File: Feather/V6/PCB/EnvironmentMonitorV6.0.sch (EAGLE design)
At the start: 64 parts, among them IC1 BME680, IC2 TCS3472, IC3 CCS811, IC5 FEATHERWING_NODIM, Q1 IRFML8244TRPBF, U1 GRIDEYE, U2 LMV358, U3 LIS3DH

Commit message: Modified mounting holes to smaller size to match enclosure.
Modified cutout so it's a larger continious section.

Updated images from DirtyPCBs

Added image exports from Eagle.

Boards updated at DirtyPCBs.
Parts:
- removed H1, H2, H3, H4, H5: MOUNT-HOLE2.8, holes:MOUNT-HOLE2.8
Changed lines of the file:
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@@
 <part name="SUPPLY10" library="SparkFun-Aesthetics" deviceset="3.3V" device=""/>
 <part name="C3" library="SparkFun-Capacitors" deviceset="1.0UF-25V-+80/-20(0805)" device="&quot;" value="1.0uF"/>
-<part name="H1" library="holes" deviceset="MOUNT-HOLE" device="2.8" value="MOUNT-HOLE2.8"/>
-<part name="H2" library="holes" deviceset="MOUNT-HOLE" device="2.8" value="MOUNT-HOLE2.8"/>
 <part name="LOGO1" library="SparkFun-Aesthetics" deviceset="OSHW-LOGO" device="M"/>
 <part name="SUPPLY14" library="SparkFun-Aesthetics" deviceset="3.3V" device=""/>
@@
 <part name="SUPPLY5" library="SparkFun-Aesthetics" deviceset="3.3V" device=""/>
 <part name="IC5" library="ThingySticks" deviceset="FEATHERWING" device="_NODIM" value="FEATHERWING_NODIM"/>
-<part name="H3" library="holes" deviceset="MOUNT-HOLE" device="2.8" value="MOUNT-HOLE2.8"/>
-<part name="H4" library="holes" deviceset="MOUNT-HOLE" device="2.8" value="MOUNT-HOLE2.8"/>
 <part name="JP3" library="SparkFun-Connectors" deviceset="M04" device="JST-PTH-VERT" value="Serial"/>
 <part name="JP4" library="SparkFun-Connectors" deviceset="M04" device="JST-PTH-VERT" value="D7-8"/>
@@
 <part name="BT1" library="ThingySticks" deviceset="BATTERY" device="-16340"/>
 <part name="GND19" library="SparkFun-Aesthetics" deviceset="GND" device=""/>
-<part name="H5" library="holes" deviceset="MOUNT-HOLE" device="2.8" value="MOUNT-HOLE2.8"/>
 <part name="U1" library="SparkFun-Sensors" deviceset="GRIDEYE" device=""/>
 <part name="U2" library="SparkFun-IC-Amplifiers" deviceset="LMV358" device="SOIC" value="LMV358"/>
@@
 <instance part="SUPPLY10" gate="G$1" x="119.38" y="96.52"/>
 <instance part="C3" gate="G$1" x="15.24" y="160.02" rot="R180"/>
-<instance part="H1" gate="G$1" x="198.12" y="180.34"/>
-<instance part="H2" gate="G$1" x="198.12" y="175.26"/>
 <instance part="LOGO1" gate="G$1" x="218.44" y="129.54"/>
 <instance part="SUPPLY14" gate="G$1" x="15.24" y="165.1"/>
@@
 <instance part="SUPPLY5" gate="G$1" x="66.04" y="165.1"/>
 <instance part="IC5" gate="G$1" x="66.04" y="99.06" rot="R270"/>
-<instance part="H3" gate="G$1" x="223.52" y="180.34"/>
-<instance part="H4" gate="G$1" x="223.52" y="175.26"/>
 <instance part="JP3" gate="G$1" x="236.22" y="55.88" rot="R180"/>
 <instance part="JP4" gate="G$1" x="236.22" y="96.52" rot="R180"/>
@@
 <instance part="BT1" gate="G$1" x="127" y="22.86"/>
 <instance part="GND19" gate="1" x="139.7" y="15.24"/>
-<instance part="H5" gate="G$1" x="198.12" y="170.18"/>
 <instance part="U1" gate="U1" x="68.58" y="20.32"/>
 <instance part="U2" gate="G1" x="-43.18" y="116.84"/>

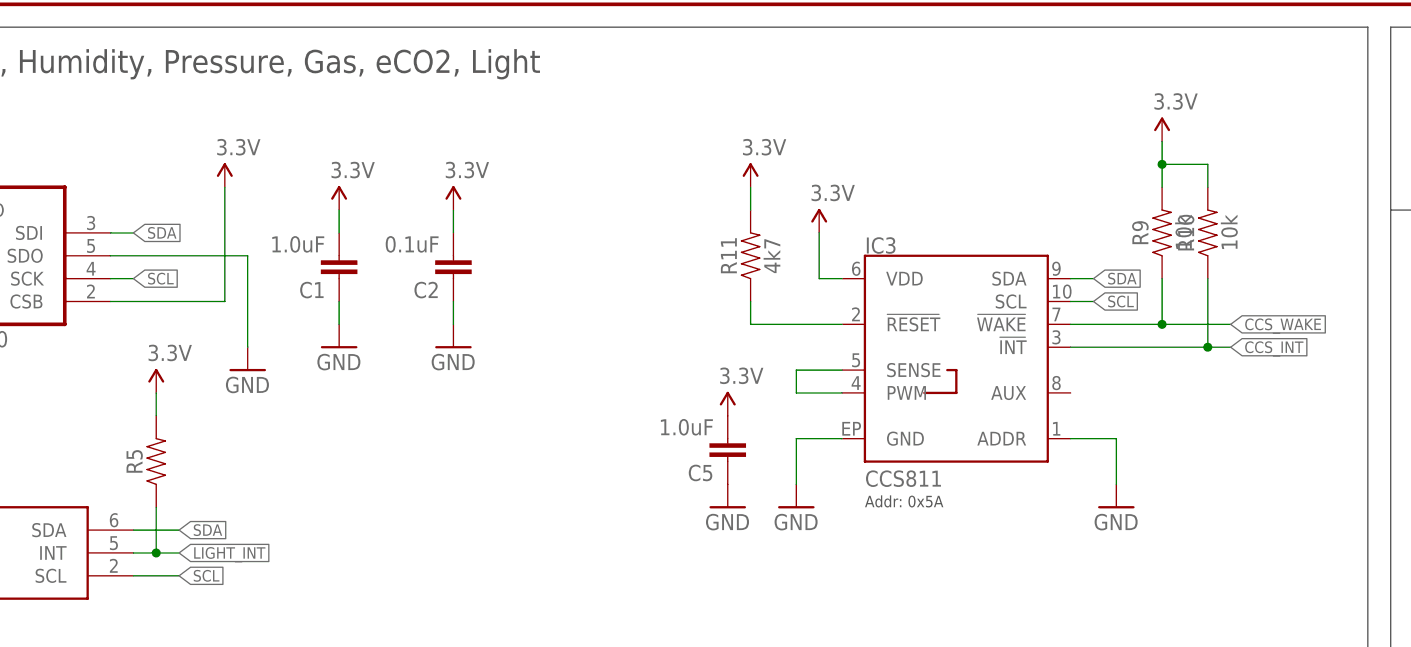
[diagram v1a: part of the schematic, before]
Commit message: Added values and corrected filename for export script
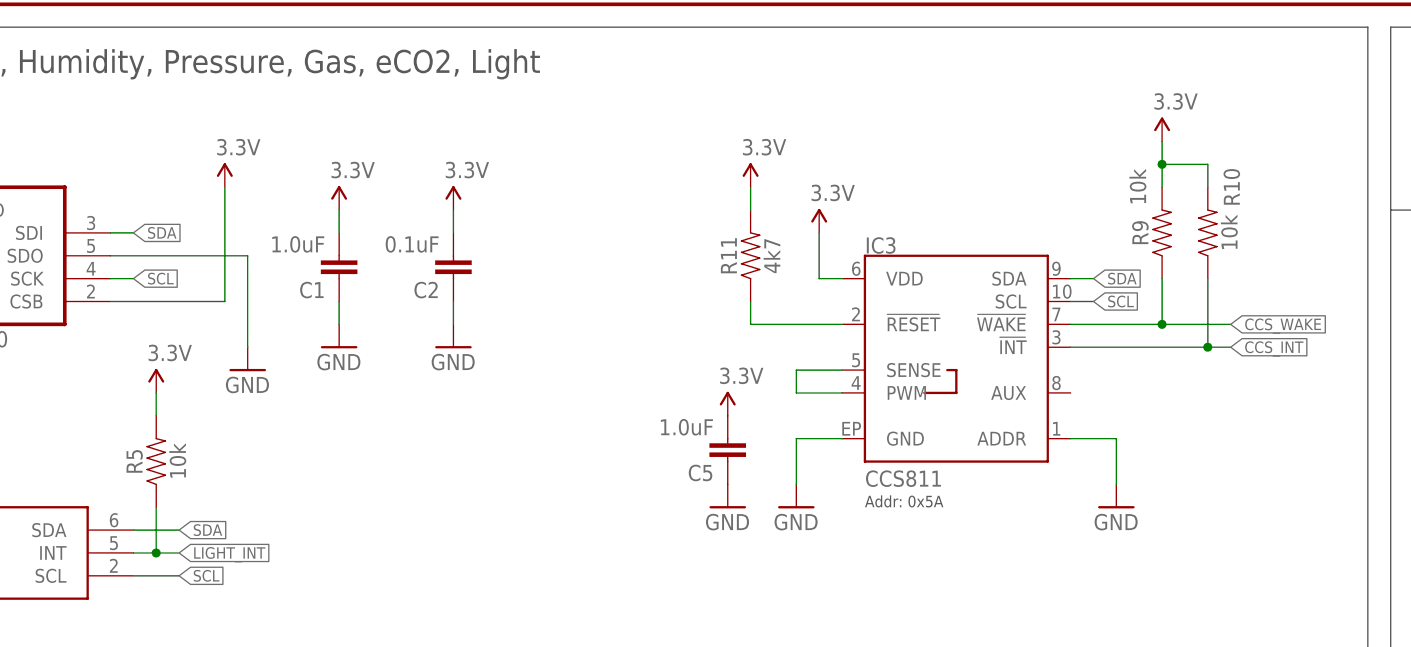
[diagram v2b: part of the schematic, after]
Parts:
- R5: value (none) -> 10k
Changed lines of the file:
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@@
 <part name="GND11" library="SparkFun-Aesthetics" deviceset="GND" device=""/>
 <part name="SUPPLY11" library="SparkFun-Aesthetics" deviceset="3.3V" device=""/>
-<part name="R5" library="SparkFun-Resistors" deviceset="RESISTOR" device="0805" value=" "/>
+<part name="R5" library="SparkFun-Resistors" deviceset="RESISTOR" device="0805" value="10k"/>
 <part name="SUPPLY12" library="SparkFun-Aesthetics" deviceset="3.3V" device=""/>
 <part name="SUPPLY5" library="SparkFun-Aesthetics" deviceset="3.3V" device=""/>
@@
 <instance part="SUPPLY6" gate="G$1" x="121.92" y="139.7"/>
 <instance part="GND23" gate="1" x="121.92" y="129.54"/>
-<instance part="R9" gate="G$1" x="170.18" y="160.02" rot="R90"/>
-<instance part="R10" gate="G$1" x="175.26" y="160.02" rot="R90"/>
+<instance part="R9" gate="G$1" x="170.18" y="160.02" smashed="yes" rot="R90">
+<attribute name="NAME" x="168.656" y="160.02" size="1.778" layer="95" font="vector" rot="R90" align="bottom-center"/>
+<attribute name="VALUE" x="166.624" y="165.1" size="1.778" layer="96" font="vector" rot="R90" align="top-center"/>
+</instance>
+<instance part="R10" gate="G$1" x="175.26" y="160.02" smashed="yes" rot="R90">
+<attribute name="NAME" x="178.816" y="165.1" size="1.778" layer="95" font="vector" rot="R90" align="bottom-center"/>
+<attribute name="VALUE" x="176.784" y="160.02" size="1.778" layer="96" font="vector" rot="R90" align="top-center"/>
+</instance>
 <instance part="SUPPLY13" gate="G$1" x="170.18" y="170.18"/>
 <instance part="R11" gate="G$1" x="124.46" y="157.48" rot="R90"/>
